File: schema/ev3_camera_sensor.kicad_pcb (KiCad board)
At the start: 2 copper layers, 39.4 x 64.8 mm, 20 parts

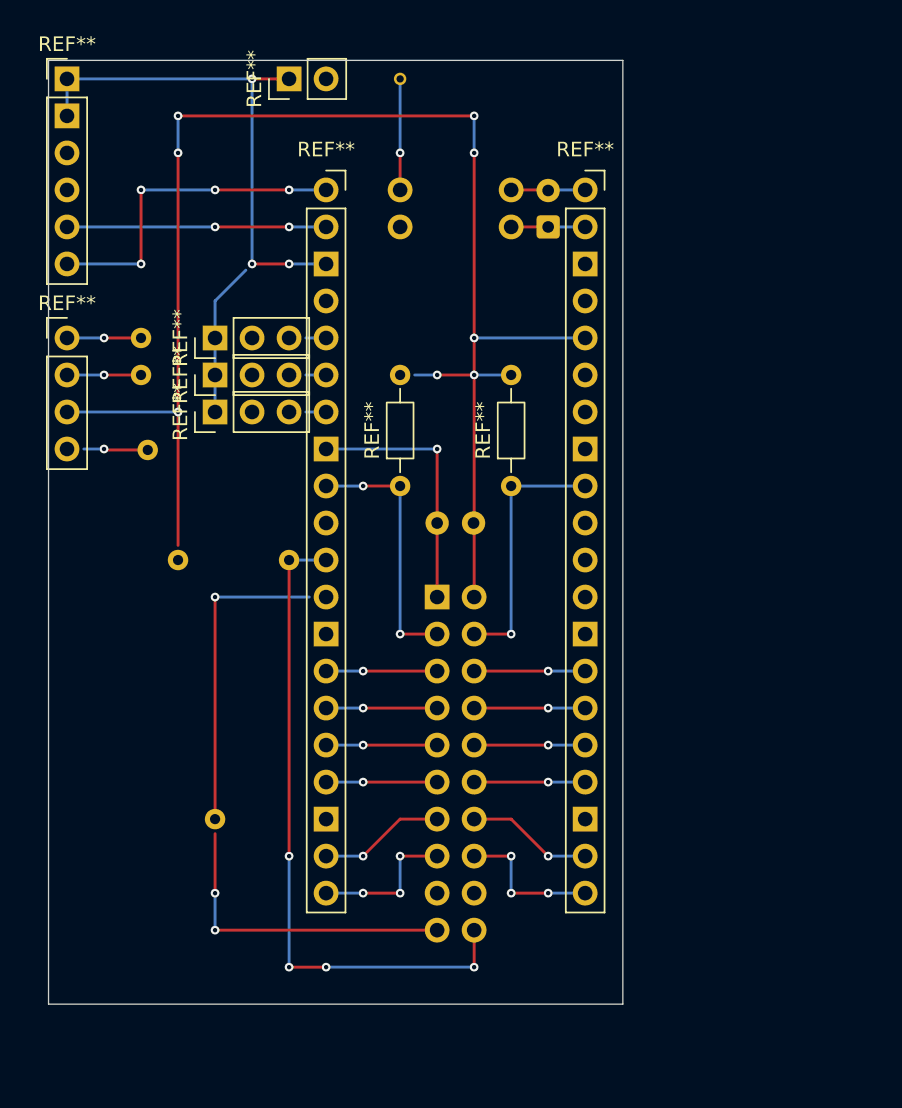
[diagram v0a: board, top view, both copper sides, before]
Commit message: change LED chip
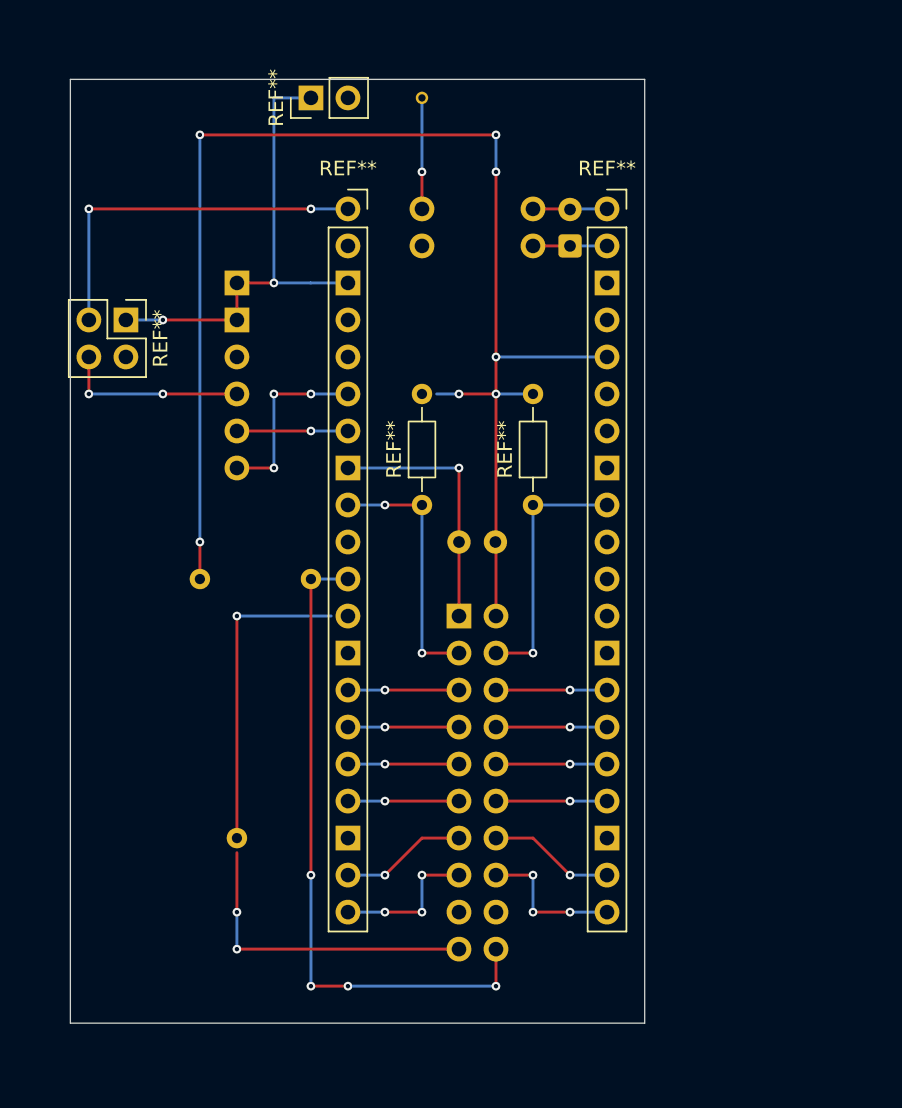
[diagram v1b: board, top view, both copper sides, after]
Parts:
- removed the REF** at (134.4, 87.6)
- removed the REF** at (129.3, 85.1)
- removed the REF** at (129.3, 82.5)
- removed the REF** at (136.9, 87.6)
- removed the REF** at (124.2, 82.5)
- removed the REF** at (134.4, 85.1)
- removed the REF** at (134.4, 82.5)
- added REF**: PinHeader_2x02_P2.54mm_Vertical, Connector_PinHeader_2.54mm:PinHeader_2x02_P2.54mm_Vertical, F.Cu at (128.3, 81.3)
- REF**: moved to B.Cu
- moved REF** 17.6 mm to (135.9, 77.9), turned to 180 degrees
- moved REF** 1.99 mm to (158.8, 76.2)
- moved REF** 1.99 mm to (141.0, 66.0)
- moved REF** 1.99 mm to (148.6, 94.0)
- moved REF** 1.99 mm to (156.2, 94.0)
- moved REF** 1.99 mm to (148.6, 66.0)
- moved REF** 1.99 mm to (156.2, 73.7)
- moved REF** 1.99 mm to (135.9, 116.8)
- moved REF** 1.99 mm to (133.3, 99.1)
- moved REF** 1.99 mm to (161.3, 73.7)
- moved REF** 1.99 mm to (153.6, 96.5)
- moved REF** 1.99 mm to (151.1, 101.6)
- moved REF** 1.99 mm to (143.5, 73.7)
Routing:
- net (no net): track 469.3 -> 448.5 mm, vias 56 -> 50

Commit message: Update Schema
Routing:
- net (no net): track 448.5 -> 453.6 mm, vias 50 -> 52
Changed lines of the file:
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@@
 		(fp_line
 			(start 1.33 -1.27)
-			(end 1.33 -24.19)
+			(end 1.33 -21.59)
 			(stroke
 				(width 0.12)
@@
 		(fp_line
 			(start -3.87 1.33)
-			(end -3.87 -24.19)
+			(end -3.87 -21.59)
 			(stroke
 				(width 0.12)
@@
 		)
 		(fp_line
-			(start -3.87 -24.19)
-			(end 1.33 -24.19)
+			(start -3.87 -21.59)
+			(end 1.33 -21.59)
 			(stroke
 				(width 0.12)
@@
 		(fp_line
 			(start 1.77 1.77)
-			(end 1.77 -24.63)
+			(end 1.77 -22.225)
 			(stroke
 				(width 0.05)
@@
 		)
 		(fp_line
-			(start 1.77 -24.63)
-			(end -4.31 -24.63)
+			(start 1.77 -22.225)
+			(end -4.31 -22.225)
 			(stroke
 				(width 0.05)
@@
 		)
 		(fp_line
-			(start -4.31 -24.63)
+			(start -4.31 -22.225)
 			(end -4.31 1.77)
 			(stroke
@@
 		)
 		(fp_rect
-			(start -4.5 3.75)
-			(end 27.27 -26.75)
+			(start -4.5 7.46)
+			(end 30.67 -27.94)
 			(stroke
 				(width 0.05)
@@
 		(fp_line
 			(start 1.27 0.27)
-			(end 1.27 -24.13)
+			(end 1.27 -21.59)
 			(stroke
 				(width 0.1)
@@
 		)
 		(fp_line
-			(start 1.27 -24.13)
-			(end -3.81 -24.13)
+			(start 1.27 -21.59)
+			(end -3.81 -21.59)
 			(stroke
 				(width 0.1)
@@
 		)
 		(fp_line
-			(start -3.81 -24.13)
+			(start -3.81 -21.59)
 			(end -3.81 1.27)
 			(stroke
@@
 		(pad "18" thru_hole circle
 			(at 0 -20.32 180)
-			(size 1.7 1.7)
-			(drill 1)
-			(layers "*.Cu" "*.Mask")
-			(remove_unused_layers no)
-		)
-		(pad "19" thru_hole circle
-			(at -2.54 -22.86 180)
-			(size 1.7 1.7)
-			(drill 1)
-			(layers "*.Cu" "*.Mask")
-			(remove_unused_layers no)
-		)
-		(pad "20" thru_hole circle
-			(at 0 -22.86 180)
 			(size 1.7 1.7)
 			(drill 1)
@@
 	)
 	(segment
-		(start 151.13 124.46)
-		(end 135.89 124.46)
-		(width 0.2)
-		(layer "F.Cu")
-		(net "")
-	)
-	(segment
 		(start 153.67 116.84)
 		(end 156.21 116.84)
@@
 	)
 	(segment
+		(start 143.51 124.46)
+		(end 135.89 124.46)
+		(width 0.2)
+		(layer "F.Cu")
+		(net "")
+	)
+	(segment
 		(start 151.13 119.38)
 		(end 148.59 119.38)
@@
 	)
 	(segment
-		(start 153.67 124.46)
-		(end 153.67 127)
-		(width 0.2)
-		(layer "F.Cu")
-		(net "")
-	)
-	(segment
 		(start 153.67 111.76)
 		(end 158.75 111.76)
@@
 	)
 	(segment
+		(start 151.13 121.92)
+		(end 151.13 124.46)
+		(width 0.2)
+		(layer "F.Cu")
+		(net "")
+	)
+	(segment
 		(start 153.67 114.3)
 		(end 158.75 114.3)
@@
 	)
 	(segment
+		(start 153.67 127)
+		(end 153.67 121.92)
+		(width 0.2)
+		(layer "F.Cu")
+		(net "")
+	)
+	(segment
 		(start 151.13 101.6)
 		(end 151.13 91.44)
@@
 	)
 	(via
+		(at 151.13 124.46)
+		(size 0.6)
+		(drill 0.3)
+		(layers "F.Cu" "B.Cu")
+		(net "")
+	)
+	(via
 		(at 148.59 104.14)
 		(size 0.6)
@@
 	)
 	(via
+		(at 156.21 119.38)
+		(size 0.6)
+		(drill 0.3)
+		(layers "F.Cu" "B.Cu")
+		(net "")
+	)
+	(via
+		(at 151.13 86.36)
+		(size 0.6)
+		(drill 0.3)
+		(layers "F.Cu" "B.Cu")
+		(net "")
+	)
+	(via
+		(at 158.75 76.2)
+		(size 0.6)
+		(drill 0.3)
+		(layers "F.Cu" "B.Cu")
+		(net "")
+	)
+	(via
+		(at 130.81 86.36)
+		(size 0.6)
+		(drill 0.3)
+		(layers "F.Cu" "B.Cu")
+		(net "")
+	)
+	(via
+		(at 146.05 93.98)
+		(size 0.6)
+		(drill 0.3)
+		(layers "F.Cu" "B.Cu")
+		(net "")
+	)
+	(via
+		(at 146.05 121.92)
+		(size 0.6)
+		(drill 0.3)
+		(layers "F.Cu" "B.Cu")
+		(net "")
+	)
+	(via
+		(at 156.21 104.14)
+		(size 0.6)
+		(drill 0.3)
+		(layers "F.Cu" "B.Cu")
+		(net "")
+	)
+	(via
+		(at 143.51 127)
+		(size 0.6)
+		(drill 0.3)
+		(layers "F.Cu" "B.Cu")
+		(net "")
+	)
+	(via
+		(at 158.75 109.22)
+		(size 0.6)
+		(drill 0.3)
+		(layers "F.Cu" "B.Cu")
+		(net "")
+	)
+	(via
+		(at 158.75 106.68)
+		(size 0.6)
+		(drill 0.3)
+		(layers "F.Cu" "B.Cu")
+		(net "")
+	)
+	(via
+		(at 138.43 78.74)
+		(size 0.6)
+		(drill 0.3)
+		(layers "F.Cu" "B.Cu")
+		(net "")
+	)
+	(via
+		(at 138.43 91.44)
+		(size 0.6)
+		(drill 0.3)
+		(layers "F.Cu" "B.Cu")
+		(net "")
+	)
+	(via
+		(at 140.97 99.06)
+		(size 0.6)
+		(drill 0.3)
+		(layers "F.Cu" "B.Cu")
+		(net "")
+	)
+	(via
+		(at 140.97 127)
+		(size 0.6)
+		(drill 0.3)
+		(layers "F.Cu" "B.Cu")
+		(net "")
+	)
+	(via
+		(at 143.51 124.46)
+		(size 0.6)
+		(drill 0.3)
+		(layers "F.Cu" "B.Cu")
+		(net "")
+	)
+	(via
+		(at 146.05 109.22)
+		(size 0.6)
+		(drill 0.3)
+		(layers "F.Cu" "B.Cu")
+		(net "")
+	)
+	(via
+		(at 140.97 73.66)
+		(size 0.6)
+		(drill 0.3)
+		(layers "F.Cu" "B.Cu")
+		(net "")
+	)
+	(via
+		(at 158.75 111.76)
+		(size 0.6)
+		(drill 0.3)
+		(layers "F.Cu" "B.Cu")
+		(net "")
+	)
+	(via
+		(at 158.75 119.38)
+		(size 0.6)
+		(drill 0.3)
+		(layers "F.Cu" "B.Cu")
+		(net "")
+	)
+	(via
 		(at 135.89 124.46)
-		(size 0.6)
-		(drill 0.3)
-		(layers "F.Cu" "B.Cu")
-		(net "")
-	)
-	(via
-		(at 156.21 119.38)
-		(size 0.6)
-		(drill 0.3)
-		(layers "F.Cu" "B.Cu")
-		(net "")
-	)
-	(via
-		(at 151.13 86.36)
-		(size 0.6)
-		(drill 0.3)
-		(layers "F.Cu" "B.Cu")
-		(net "")
-	)
-	(via
-		(at 158.75 76.2)
-		(size 0.6)
-		(drill 0.3)
-		(layers "F.Cu" "B.Cu")
-		(net "")
-	)
-	(via
-		(at 130.81 86.36)
-		(size 0.6)
-		(drill 0.3)
-		(layers "F.Cu" "B.Cu")
-		(net "")
-	)
-	(via
-		(at 146.05 93.98)
-		(size 0.6)
-		(drill 0.3)
-		(layers "F.Cu" "B.Cu")
-		(net "")
-	)
-	(via
-		(at 146.05 121.92)
-		(size 0.6)
-		(drill 0.3)
-		(layers "F.Cu" "B.Cu")
-		(net "")
-	)
-	(via
-		(at 156.21 104.14)
-		(size 0.6)
-		(drill 0.3)
-		(layers "F.Cu" "B.Cu")
-		(net "")
-	)
-	(via
-		(at 143.51 127)
-		(size 0.6)
-		(drill 0.3)
-		(layers "F.Cu" "B.Cu")
-		(net "")
-	)
-	(via
-		(at 158.75 109.22)
-		(size 0.6)
-		(drill 0.3)
-		(layers "F.Cu" "B.Cu")
-		(net "")
-	)
-	(via
-		(at 158.75 106.68)
-		(size 0.6)
-		(drill 0.3)
-		(layers "F.Cu" "B.Cu")
-		(net "")
-	)
-	(via
-		(at 138.43 78.74)
-		(size 0.6)
-		(drill 0.3)
-		(layers "F.Cu" "B.Cu")
-		(net "")
-	)
-	(via
-		(at 138.43 91.44)
-		(size 0.6)
-		(drill 0.3)
-		(layers "F.Cu" "B.Cu")
-		(net "")
-	)
-	(via
-		(at 140.97 99.06)
-		(size 0.6)
-		(drill 0.3)
-		(layers "F.Cu" "B.Cu")
-		(net "")
-	)
-	(via
-		(at 140.97 127)
-		(size 0.6)
-		(drill 0.3)
-		(layers "F.Cu" "B.Cu")
-		(net "")
-	)
-	(via
-		(at 146.05 109.22)
-		(size 0.6)
-		(drill 0.3)
-		(layers "F.Cu" "B.Cu")
-		(net "")
-	)
-	(via
-		(at 140.97 73.66)
-		(size 0.6)
-		(drill 0.3)
-		(layers "F.Cu" "B.Cu")
-		(net "")
-	)
-	(via
-		(at 158.75 111.76)
-		(size 0.6)
-		(drill 0.3)
-		(layers "F.Cu" "B.Cu")
-		(net "")
-	)
-	(via
-		(at 158.75 119.38)
 		(size 0.6)
 		(drill 0.3)
@@
 	)
 	(segment
+		(start 151.13 124.46)
+		(end 143.51 124.46)
+		(width 0.2)
+		(layer "B.Cu")
+		(net "")
+	)
+	(segment
 		(start 135.89 101.6)
 		(end 142.36 101.6)
@@
 	)
 	(segment
+		(start 148.59 71.12)
+		(end 148.59 66.04)
+		(width 0.2)
+		(layer "B.Cu")
+		(net "")
+	)
+	(segment
 		(start 135.89 124.46)
 		(end 135.89 121.92)
 		(width 0.2)
 		(layer "B.Cu")
-		(net "")
-	)
-	(segment
-		(start 148.59 71.12)
-		(end 148.59 66.04)
-		(width 0.2)
-		(layer "B.Cu")

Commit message: update pcb
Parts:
- removed the REF** at (161.3, 73.7)
- removed the REF** at (156.2, 73.7)
- removed the REF** at (128.3, 81.3)
- removed the REF** at (141.0, 66.0)
- removed the REF** at (148.6, 94.0)
- removed the REF** at (143.5, 73.7)
- removed the REF** at (156.2, 94.0)
- removed the REF** at (135.9, 116.8)
- removed the REF** at (133.3, 99.1)
- added REF**: PinSocket_1x20_P2.54mm_Vertical, Connector_PinSocket_2.54mm:PinSocket_1x20_P2.54mm_Vertical, F.Cu at (174.0, 78.7)
- added REF**: PinHeader_1x02_P2.54mm_Vertical, Connector_PinHeader_2.54mm:PinHeader_1x02_P2.54mm_Vertical, B.Cu at (168.9, 78.7)
- added REF**: R_Axial_DIN0204_L3.6mm_D1.6mm_P7.62mm_Horizontal, Resistor_THT:R_Axial_DIN0204_L3.6mm_D1.6mm_P7.62mm_Horizontal, F.Cu at (176.6, 88.9)
- added REF**: R_Axial_DIN0204_L3.6mm_D1.6mm_P7.62mm_Horizontal, Resistor_THT:R_Axial_DIN0204_L3.6mm_D1.6mm_P7.62mm_Horizontal, F.Cu at (161.3, 99.1)
- added REF**: PinHeader_1x02_P2.54mm_Vertical, Connector_PinHeader_2.54mm:PinHeader_1x02_P2.54mm_Vertical, F.Cu at (153.7, 71.1)
- added REF**: PinSocket_1x20_P2.54mm_Vertical, Connector_PinSocket_2.54mm:PinSocket_1x20_P2.54mm_Vertical, F.Cu at (156.2, 78.7)
- added REF**: R_Axial_DIN0204_L3.6mm_D1.6mm_P7.62mm_Horizontal, Resistor_THT:R_Axial_DIN0204_L3.6mm_D1.6mm_P7.62mm_Horizontal, F.Cu at (168.9, 99.1)
- added REF**: R_Axial_DIN0204_L3.6mm_D1.6mm_P7.62mm_Horizontal, Resistor_THT:R_Axial_DIN0204_L3.6mm_D1.6mm_P7.62mm_Horizontal, B.Cu at (156.3, 121.9)
- REF**: moved to F.Cu
- moved REF** 29.9 mm to (148.6, 105.0)
- moved REF** 13.7 mm to (163.8, 106.7)
- moved REF** 13.7 mm to (166.3, 101.6)
- moved REF** 13.7 mm to (171.4, 81.3)
- moved REF** 13.7 mm to (161.3, 71.1)
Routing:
- net (no net): track 453.6 -> 342.1 mm, vias 52 -> 24
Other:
- board size 39.4 x 64.8 mm -> 38.1 x 63.5 mm

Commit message: reflect removal of color led
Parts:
- added REF**: SW_PUSH_6mm, Button_Switch_THT:SW_PUSH_6mm, F.Cu at (148.6, 104.1)
- REF**: moved to B.Cu
- moved REF** 13.0 mm to (151.2, 92.3), turned to 0 degrees
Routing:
- net (no net): track 342.1 -> 361.8 mm, vias 24 -> 32
